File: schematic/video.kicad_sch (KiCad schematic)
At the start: 10 parts, among them U10 MK4116P, U11 MK4116P, U12 MK4116P, U13 MK4116P, U14 MK4116P, U15 MK4116P, U16 MK4116P, U17 MK4116P, U9 TMS9928A

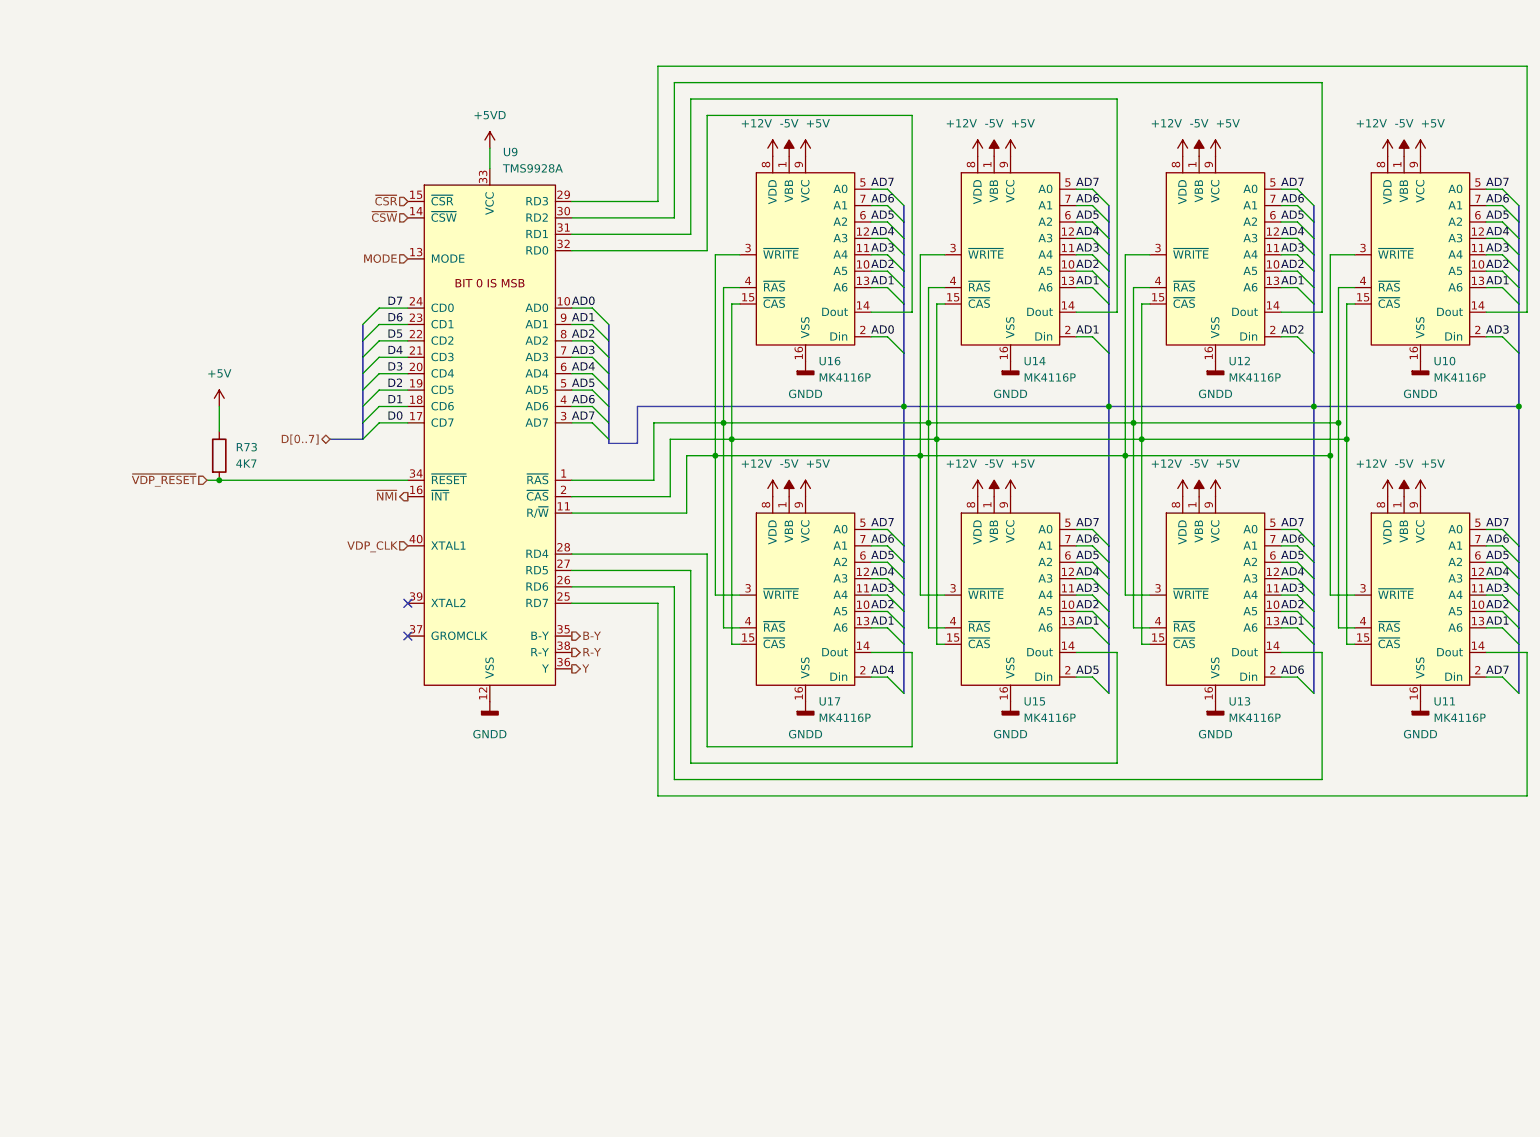
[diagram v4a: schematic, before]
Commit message: adjusted size of the sheets. added pcb version to the rev field. F.0... the 0 is for future fixes on my end. RF PCB is E.0.
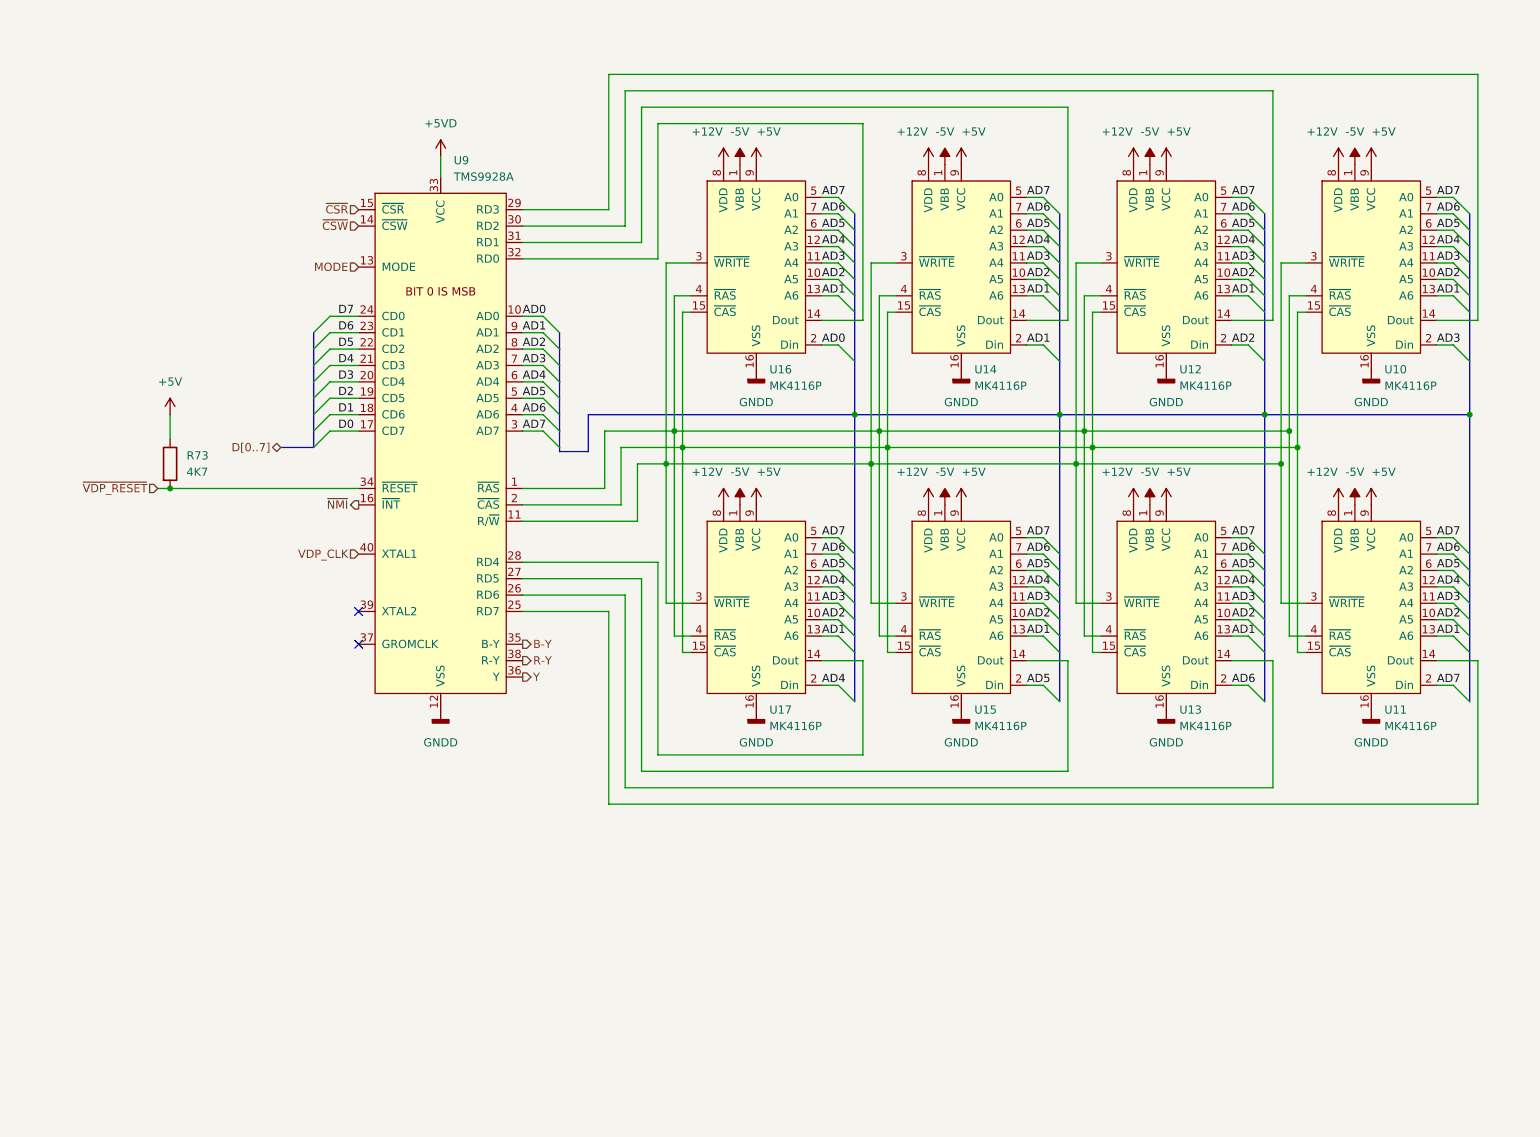
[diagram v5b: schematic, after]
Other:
- title: (none) -> Colecovision Schematic
- moved on the sheet: R73, U10, U11, U12, U13, U14, U15, U16, U17, U9

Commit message: cleanup, and started associating components
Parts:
- R73: footprint (none) -> Resistor_THT:R_Axial_DIN0207_L6.3mm_D2.5mm_P7.62mm_Horizontal
- U10, U11, U12, U13, U14, U15, U16, U17: footprint (none) -> Package_DIP:DIP-16_W7.62mm_LongPads
- U9: footprint (none) -> Package_DIP:DIP-40_W15.24mm_LongPads

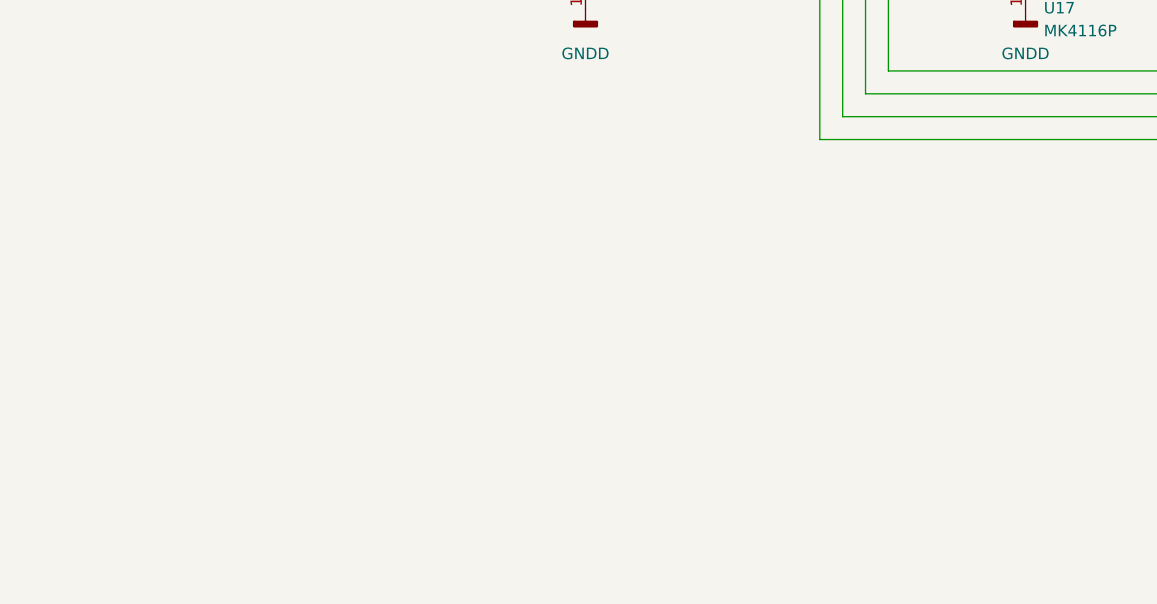
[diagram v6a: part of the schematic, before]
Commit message: first draft of board with components added, no traces
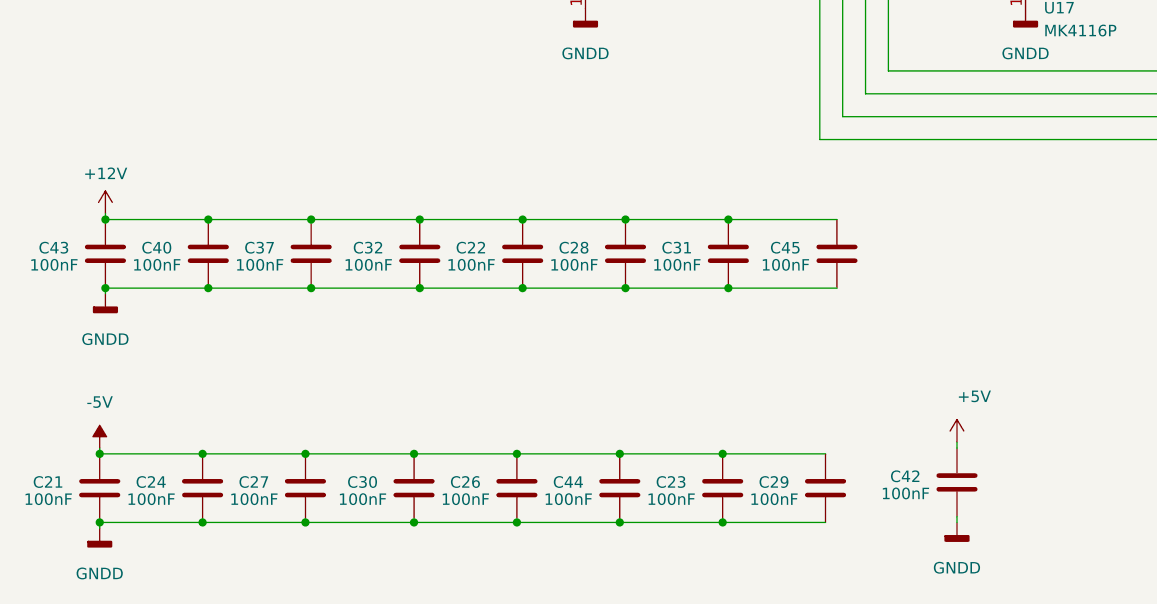
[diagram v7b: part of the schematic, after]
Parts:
- added C21, C22, C23, C24, C26, C27, C28, C29, C30, C31, C32, C37, C40, C42, C43, C44, C45: 100nF, Capacitor_THT:C_Disc_D7.0mm_W2.5mm_P5.00mm, symbol Device:C
- R73: footprint Resistor_THT:R_Axial_DIN0207_L6.3mm_D2.5mm_P7.62mm_Horizontal -> Resistor_THT:R_Axial_DIN0207_L6.3mm_D2.5mm_P10.16mm_Horizontal
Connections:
- net +12V: now also C22.1, C28.1, C31.1, C32.1, C37.1, C40.1, C43.1, C45.1
- net +5V: now also C42.1
- net -5V: now also C21.1, C23.1, C24.1, C26.1, C27.1, C29.1, C30.1, C44.1
- net GNDD: now also C21.2, C22.2, C23.2, C24.2, C26.2, C27.2, C28.2, C29.2, C30.2, C31.2, C32.2, C37.2, C40.2, C42.2, C43.2, C44.2, C45.2

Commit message: updated schematic with new layout
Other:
- company: (none) -> sparkletron
- title: Colecovision Schematic -> Reverse Engineer Colecovision
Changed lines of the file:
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@@
   (paper "USLetter")
   (title_block
-    (title "Colecovision Schematic")
-    (date "2023-01-09")
-    (rev "F.0")
+    (title "Reverse Engineer Colecovision")
+    (date "2023-03-14")
+    (rev "DEV")
+    (company "sparkletron")
     (comment 1 "Jay Convertino")
+    (comment 2 "MIT LICENSE")
   )
   (junction (at 39.37 100.965) (diameter 0) (color 0 0 0 0)
